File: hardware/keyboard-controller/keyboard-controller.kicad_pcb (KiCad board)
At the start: 2 copper layers, 80 x 101.6 mm, 30 parts, among them J1 Keybed_Connector, J2 Debug_Pins, J3 Barrel_Jack_Switch, J4 CV_OUT, J5 GATE_OUT, U1 L78L09_TO92, U2 LM358, U3 74HC164, U4 74HC164, U5 LM1117-3.3, U6 Pico, U7 TL431LP, U8 MCP4921

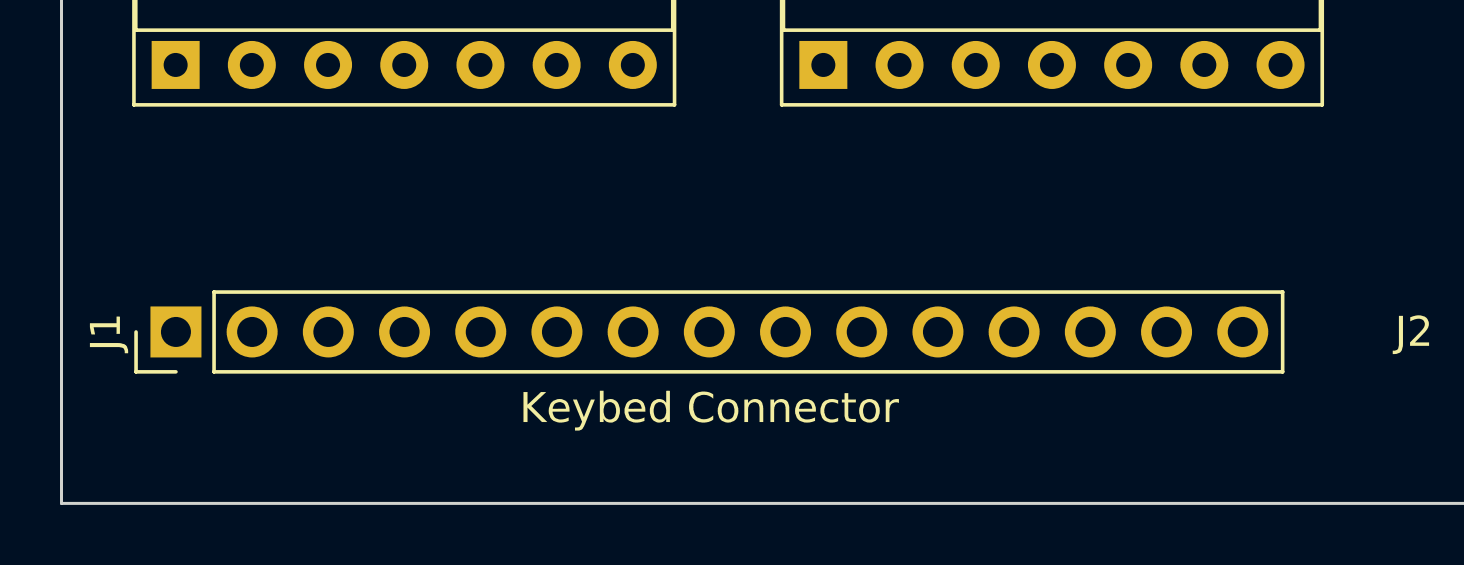
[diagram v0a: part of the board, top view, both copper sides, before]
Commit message: Code cleanup. Switched keyboard connector to 16pin IDC
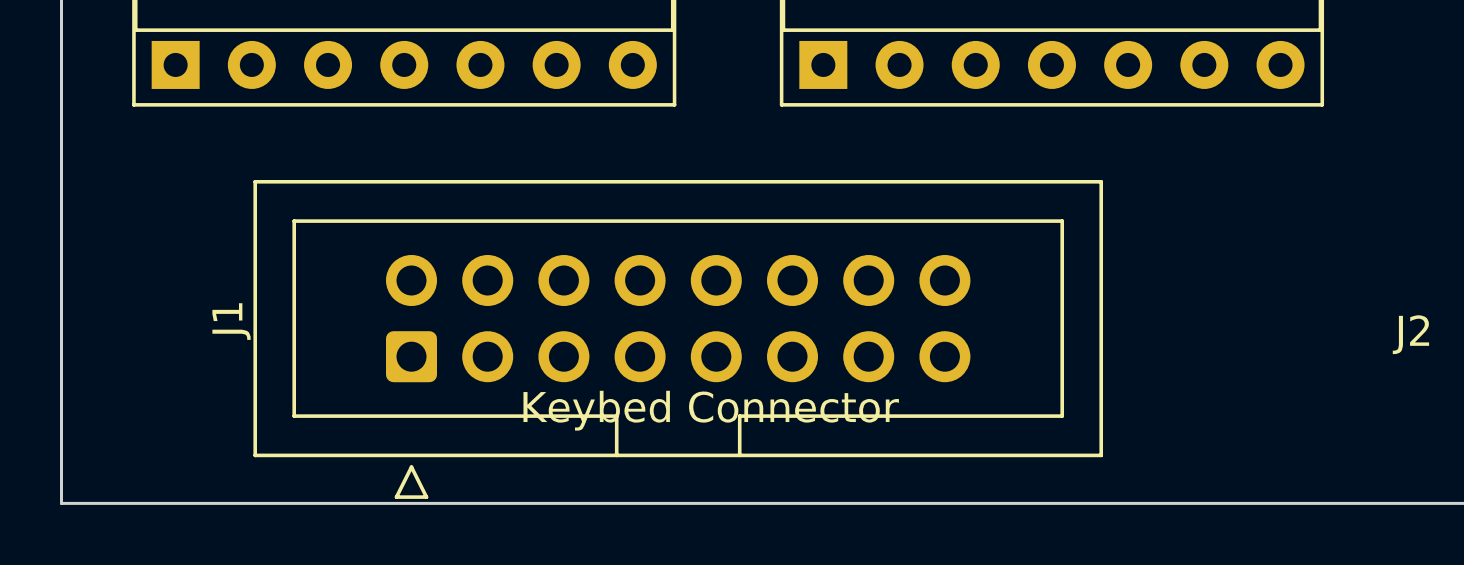
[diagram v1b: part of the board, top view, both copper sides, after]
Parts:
- J1: footprint Connector_PinHeader_2.54mm:PinHeader_1x15_P2.54mm_Vertical -> Connector_IDC:IDC-Header_2x08_P2.54mm_Vertical
- moved J1 7.90 mm to (115.1, 135.4)
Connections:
- U6 pad 10: Net-(U3-Pad1) -> unconnected-(U6-Pad10)
- U6 pad 14: MATRIX_R6 -> Net-(U6-Pad14)
- U6 pad 15: MATRIX_R5 -> Net-(U6-Pad15)
- U6 pad 16: MATRIX_R4 -> unconnected-(U6-Pad16)
- U6 pad 17: MATRIX_R3 -> Net-(U6-Pad17)
- U6 pad 19: MATRIX_R2 -> unconnected-(U6-Pad19)
- U6 pad 20: MATRIX_R1 -> unconnected-(U6-Pad20)
- U6 pad 21: unconnected-(U6-Pad21) -> MATRIX_R1
- U6 pad 22: unconnected-(U6-Pad22) -> MATRIX_R2
- U6 pad 24: Net-(U6-Pad24) -> MATRIX_R3
- U6 pad 25: unconnected-(U6-Pad25) -> MATRIX_R4
- U6 pad 26: Net-(U6-Pad26) -> MATRIX_R5
- U6 pad 27: Net-(U6-Pad27) -> MATRIX_R6
- U6 pad 29: unconnected-(U6-Pad29) -> Net-(U3-Pad1)
- U6 pad 31: unconnected-(U6-Pad31) -> Net-(U3-Pad8)
- U6 pad 34: Net-(U2-Pad5) -> unconnected-(U6-Pad34)
- U6 pad 7: unconnected-(U6-Pad7) -> Net-(U2-Pad5)
- U6 pad 9: Net-(U3-Pad8) -> unconnected-(U6-Pad9)
- U8 pad 2: Net-(U6-Pad24) -> Net-(U6-Pad17)
- U8 pad 3: Net-(U6-Pad27) -> Net-(U6-Pad14)
- U8 pad 4: Net-(U6-Pad26) -> Net-(U6-Pad15)

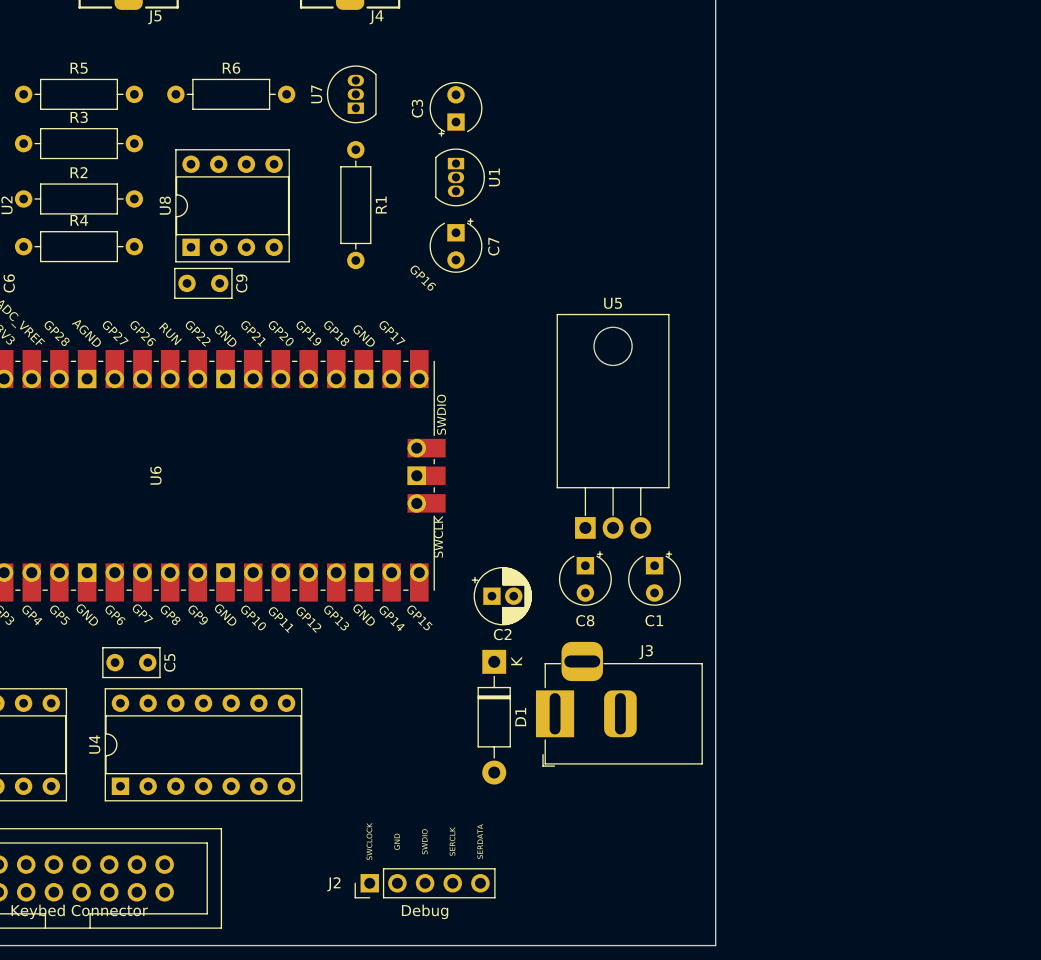
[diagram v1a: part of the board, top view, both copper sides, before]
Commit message: Tidied schematic
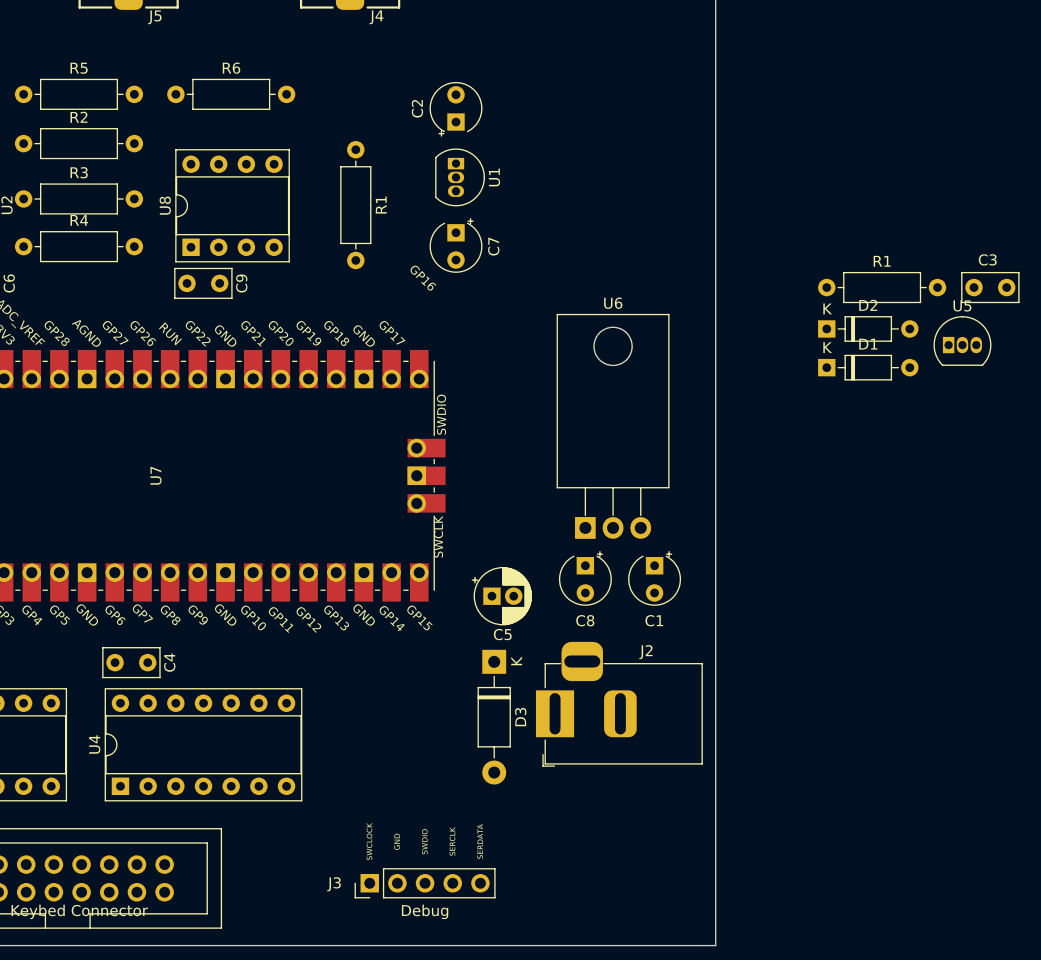
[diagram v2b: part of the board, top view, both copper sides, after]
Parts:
- removed the U7 at (150.4, 63.4)
- added C3: 0.1uF, AEC_Capacitors:C_Disc_D5.0mm_W2.5mm_P3.0mm, F.Cu at (207.1, 79.9)
- added D1: 1N4148, Diode_THT:D_DO-35_SOD27_P7.62mm_Horizontal, F.Cu at (193.6, 87.2)
- added D2: 1N4148, Diode_THT:D_DO-35_SOD27_P7.62mm_Horizontal, F.Cu at (193.6, 83.7)
- added R1: 100, Royal_Ohm_Resistors:R_Axial_DIN0207_L6.8mm_D2.5mm_P10.16mm_Horizontal, F.Cu at (193.6, 79.9)
- added U5: TL431LP, Package_TO_SOT_THT:TO-92_Inline, F.Cu at (204.8, 85.2)
- renumbered C3 to C2, C5 to C4, C2 to C5, D1 to D3, J3 to J2, J2 to J3, R3 to R2, R2 to R3, U5 to U6, U6 to U7
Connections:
- net Net-(U2-Pad3) renamed CV
- net Net-(U2-Pad5) renamed GATE
- net Net-(U3-Pad1) renamed SHIFT_DATA
- net Net-(U3-Pad8) renamed SHIFT_CLK
- net Net-(U6-Pad14) renamed SPI_CLK
- net Net-(U6-Pad15) renamed SPI_DATA
- net Net-(U6-Pad17) renamed DAC_CS
- U8 pad 6: Net-(R1-Pad1) -> VREF

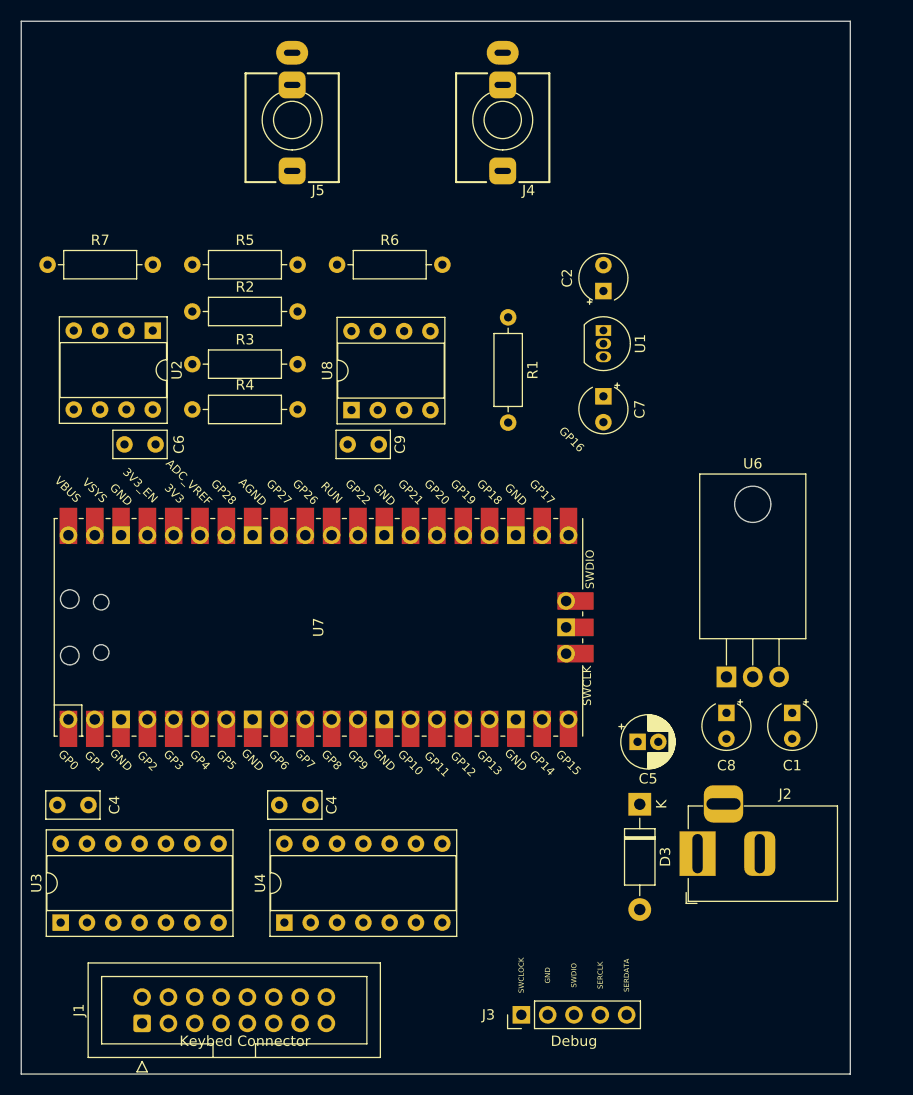
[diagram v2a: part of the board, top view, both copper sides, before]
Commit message: Added more IO
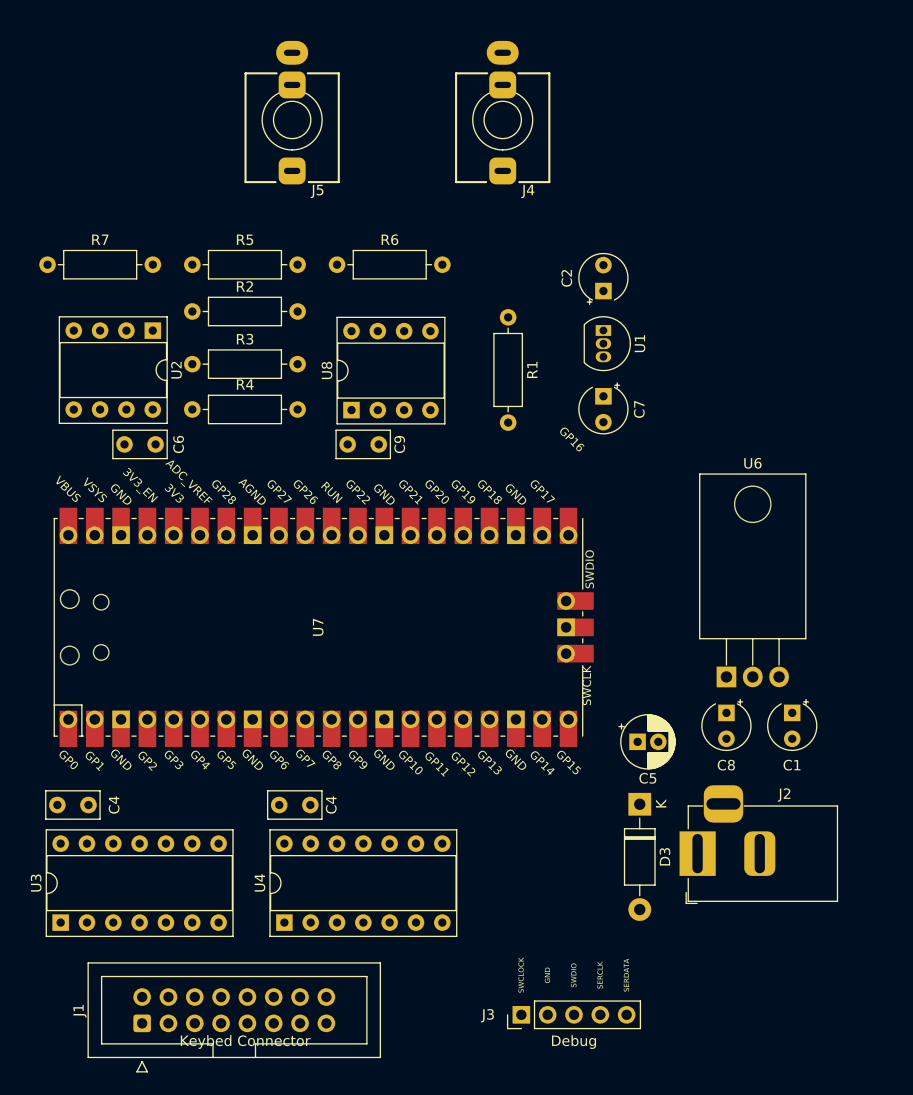
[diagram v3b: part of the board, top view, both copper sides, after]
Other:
- board outline removed
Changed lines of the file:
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@@
     )
   )
-  (gr_rect (start 103.395 38.662712) (end 183.405 140.262712) (layer "Edge.Cuts") (width 0.1) (fill none))
   (gr_text "SWDIO" (at 156.735 130.737712 90) (layer "F.SilkS")
     (effects (font (size 0.5 0.5) (thickness 0.075)))
